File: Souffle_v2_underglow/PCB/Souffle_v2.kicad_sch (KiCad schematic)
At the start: 88 parts, among them J1 LED, J2 4PIN, J3 OLED, SW1 SW_PUSH, SW10 SW_PUSH, SW11 SW_PUSH, SW12 SW_PUSH, SW13 SW_PUSH, SW14 SW_PUSH, SW15 SW_PUSH, SW16 SW_PUSH, SW17 SW_PUSH, SW18 SW_PUSH, SW19 SW_PUSH, SW2 SW_PUSH, SW20 SW_PUSH, SW21 SW_PUSH, SW22 SW_PUSH, SW23 SW_PUSH, SW24 SW_PUSH, SW25 SW_PUSH, SW25b1 RotaryEncoder_Switch, SW26 SW_PUSH, SW27 SW_PUSH, SW28 SW_PUSH, SW29 SW_PUSH, SW3 SW_PUSH, SW30 SW_PUSH, SW4 SW_PUSH, SW5 SW_PUSH, SW6 SW_PUSH, SW7 SW_PUSH, SW8 SW_PUSH, SW9 SW_PUSH, U1 ProMicro

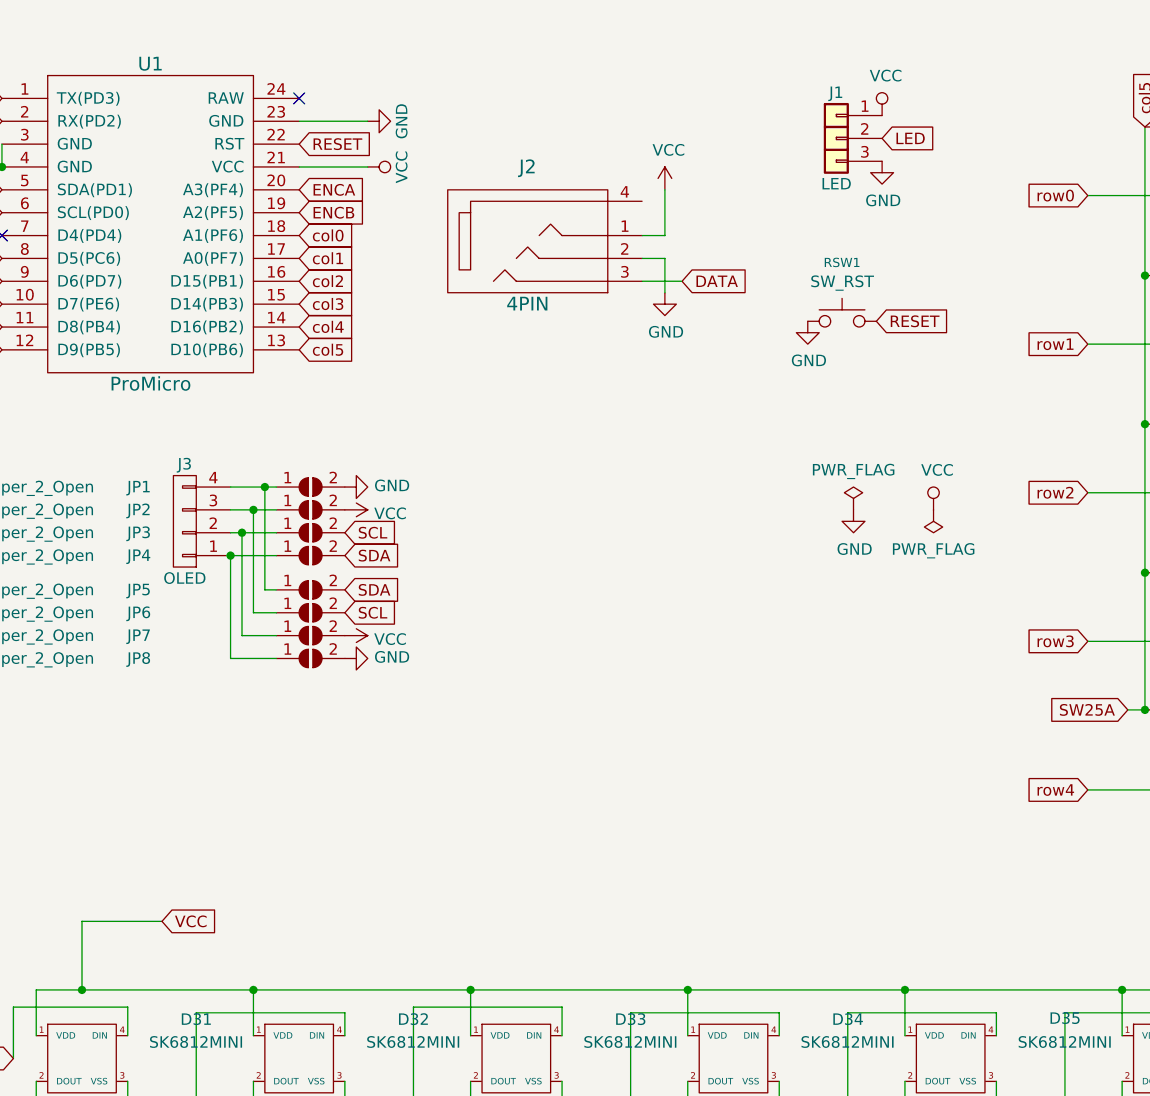
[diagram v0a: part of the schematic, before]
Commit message: LED placement and VCC pad for electricity supply to LEDs.
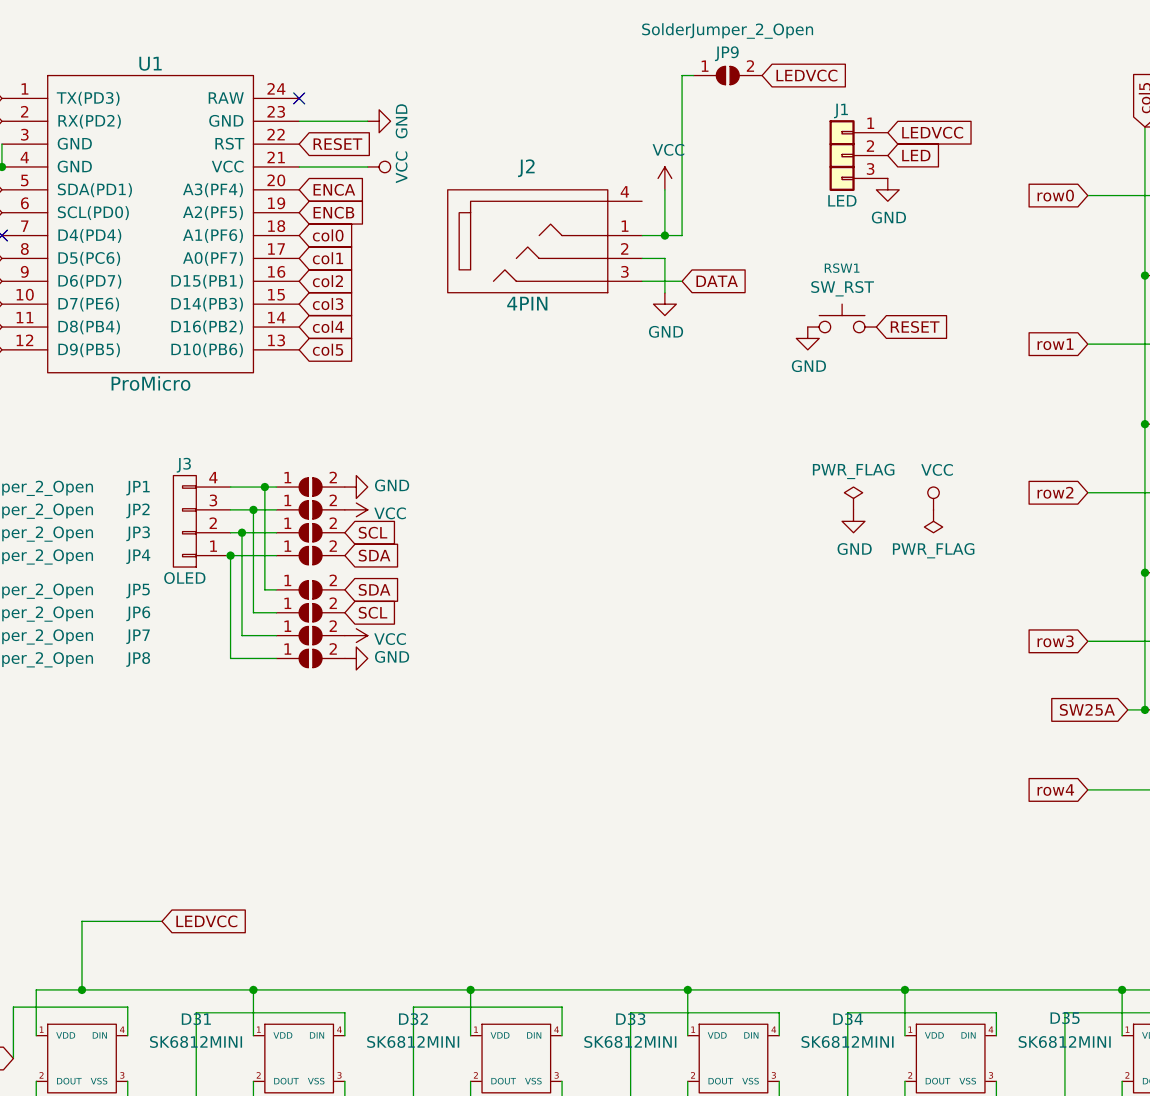
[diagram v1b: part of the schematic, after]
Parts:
- added JP9: SolderJumper_2_Open, footprints:Jumper, symbol Jumper:SolderJumper_2_Open
- JP1, JP2, JP4, JP5, JP6, JP7, JP8: footprint Jumper:SolderJumper-2_P1.3mm_Open_Pad1.0x1.5mm -> SofleKeyboard-footprint:Jumper
- JP3: footprint (none) -> SofleKeyboard-footprint:Jumper
- SW1, SW10, SW11, SW12, SW13, SW14, SW15, SW16, SW17, SW18, SW19, SW2, SW20, SW21, SW22, SW23, SW24, SW27, SW28, SW29, SW3, SW30, SW4, SW5, SW6, SW7, SW8, SW9: footprint SofleKeyboard-footprint:CherryMX_KailhLowProfile_Hotswap -> SofleKeyboard-footprint:CherryMX_Hotswap_mod
- SW25: footprint SofleKeyboard-footprint:CherryMX_KailhLowProfile_Hotswap_1.5 -> SofleKeyboard-footprint:CherryMX_Hotswap_mod
- SW26: footprint SofleKeyboard-footprint:CherryMX_KailhLowProfile_Hotswap_1.5 -> SofleKeyboard-footprint:CherryMX_Hotswap_1.5_mod
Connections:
- net VCC: now also JP9.1 (A); no longer D31.1 (VDD), D32.1 (VDD), D33.1 (VDD), D34.1 (VDD), D35.1 (VDD), D36.1 (VDD), D37.1 (VDD), J1.1 (Pin_1)
- new net LEDVCC: D31.1 (VDD), D32.1 (VDD), D33.1 (VDD), D34.1 (VDD), D35.1 (VDD), D36.1 (VDD), D37.1 (VDD), J1.1 (Pin_1), JP9.2 (B)
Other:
- moved on the sheet: J1, RSW1
